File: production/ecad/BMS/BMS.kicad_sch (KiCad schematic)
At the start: 0 parts

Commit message: schematic draft merged w neha
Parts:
- added C1: 10u, Capacitor_SMD:C_0805_2012Metric, symbol Device:C
- added C2: 22u, Capacitor_SMD:C_0805_2012Metric, symbol Device:C
- added F1: 5A, Fuse:Fuse_0805_2012Metric, symbol Device:Fuse
- added J7, J9: Conn_01x02_Pin, Connector_PinHeader_2.54mm:PinHeader_1x02_P2.54mm_Vertical, symbol Connector:Conn_01x02_Pin
- added J8: XT60PW-M, CSTAR-MainBoard-Footprints:AMASS_XT60PW-M, symbol XT60PW-M:XT60PW-M
- added LED1, LED2: 150080VS75000, CSTAR-MainBoard-Footprints:LED_0VS75000_WRE, symbol 2024-02-25_19-51-49:150080VS75000
- added R1: 600, Resistor_SMD:R_0805_2012Metric, symbol Device:R_Small
- added R2: 260, Resistor_SMD:R_0805_2012Metric, symbol Device:R_Small
- added TP1: P5V, TestPoint:TestPoint_Pad_D2.0mm, symbol Connector:TestPoint
- added TP2: P3V3, TestPoint:TestPoint_Pad_D2.0mm, symbol Connector:TestPoint
- added U2: AZ1117IH-3.3TRG1, CSTAR-MainBoard-Footprints:SOT230P700X185-4N, symbol 2024-02-15_17-38-45:AZ1117IH-3.3TRG1
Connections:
- new net: C1.1, J9.1 (Pin_1), TP1.1, U2.3 (INPUT)
- new net: LED2.2, R2.2
- new net: LED1.2, R1.2
- new net: J7.2 (Pin_2), U2.4 (Vout)
- new net: F1.2, J9.2 (Pin_2)
- new net 3V3EXT: C2.1, J7.1 (Pin_1), R2.1, TP2.1, U2.2 (OUTPUT)
- new net 5VEXT: F1.1, R1.1
- new net BATT_IN: J8.1 (+)
- new net GND: C1.2, C2.2, LED1.1, LED2.1, U2.1 (GND)
- new net GNDEXT: J8.2 (-)
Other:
- removed sheet Power Sheet
- note added: "Add large resistors for LEDs for proper power dissipation in layout"
- note added: "Battery Connector"
- note added: "Green LED"
- note added: "LDO: 5V to 3.3V, 1A"
- note added: "Protection Circutry: Two 5A Protection Fuses to the 5V and 3v3 power rails. TVS Diode"

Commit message: feedback from Billayyy
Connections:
- net GNDEXT is gone; now on net GND: J8.2 (-)
- net 5VEXT renamed +5V
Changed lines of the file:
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@@
+	(wire
+		(pts
+			(xy 186.69 53.34) (xy 186.69 59.69)
+		)
+		(stroke
+			(width 0)
+			(type default)
+		)
+	)
 	(wire
 		(pts
@@
 		)
 	)
-	(hierarchical_label "GNDEXT"
+	(hierarchical_label "5VEXT"
+		(shape output)
+		(at 186.69 59.69 270)
+		(fields_autoplaced yes)
+		(effects
+			(font
+				(size 1.27 1.27)
+			)
+			(justify right)
+		)
+	)
+	(hierarchical_label "GND"
 		(shape input)
 		(at 41.91 125.73 270)
@@
 		)
 	)
+	(symbol
+		(lib_id "power:+5V")
+		(at 186.69 53.34 0)
+		(unit 1)
+		(exclude_from_sim no)
+		(in_bom yes)
+		(on_board yes)
+		(dnp no)
+		(fields_autoplaced yes)
+		(property "Reference" "#PWR08"
+			(at 186.69 57.15 0)
+			(effects
+				(font
+					(size 1.27 1.27)
+				)
+				(hide yes)
+			)
+		)
+		(property "Value" "+5V"
+			(at 186.69 48.26 0)
+			(effects
+				(font
+					(size 1.27 1.27)
+				)
+			)
+		)
+		(property "Footprint" ""
+			(at 186.69 53.34 0)
+			(effects
+				(font
+					(size 1.27 1.27)
+				)
+				(hide yes)
+			)
+		)
+		(property "Datasheet" ""
+			(at 186.69 53.34 0)
+			(effects
+				(font
+					(size 1.27 1.27)
+				)
+				(hide yes)
+			)
+		)
+		(property "Description" "Power symbol creates a global label with name \"+5V\""
+			(at 186.69 53.34 0)
+			(effects
+				(font
+					(size 1.27 1.27)
+				)
+				(hide yes)
+			)
+		)
+		(pin "1"
+		)
+		(instances
+			(project ""
+				(path "/a34d77bc-8f6a-417e-a206-3165e6c5c658/8907b1b2-1248-4544-8d7d-33764869f691"
+					(reference "#PWR08")
+					(unit 1)
+				)
+			)
+		)
+	)

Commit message: neha bms additions
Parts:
- removed F1: 5A, Fuse:Fuse_0805_2012Metric, symbol Device:Fuse
- removed J7, J9: Conn_01x02_Pin, Connector_PinHeader_2.54mm:PinHeader_1x02_P2.54mm_Vertical, symbol Connector:Conn_01x02_Pin
- removed J8: XT60PW-M, CSTAR-MainBoard-Footprints:AMASS_XT60PW-M, symbol XT60PW-M:XT60PW-M
- removed LED1, LED2: 150080VS75000, CSTAR-MainBoard-Footprints:LED_0VS75000_WRE, symbol 2024-02-25_19-51-49:150080VS75000
- removed R1: 600, Resistor_SMD:R_0805_2012Metric, symbol Device:R_Small
- removed R2: 260, Resistor_SMD:R_0805_2012Metric, symbol Device:R_Small
- removed TP1: P5V, TestPoint:TestPoint_Pad_D2.0mm, symbol Connector:TestPoint
- removed TP2: P3V3, TestPoint:TestPoint_Pad_D2.0mm, symbol Connector:TestPoint
- removed U2: AZ1117IH-3.3TRG1, CSTAR-MainBoard-Footprints:SOT230P700X185-4N, symbol 2024-02-15_17-38-45:AZ1117IH-3.3TRG1
- added R1: 30.1k, symbol Device:R
- added R2: 53.6k, symbol Device:R
- added R3: 250k, symbol Device:R
- added U3: TPS75233QPWPREP, TPS75233QPWPREP:TPS75233QPWPREP, symbol TPS75233QPWPREP:TPS75233QPWPREP
- C1: value 10u -> 47 uF; footprint Capacitor_SMD:C_0805_2012Metric -> (none)
- C2: value 22u -> 0.22 uF; footprint Capacitor_SMD:C_0805_2012Metric -> (none)
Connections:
- net 3V3EXT is gone; now on net +5V: C2.1
- net +5V: now also U3.P$3 (IN1), U3.P$4 (IN2)
- net GND: now also R2.2, U3.P$1 (GND/HEATSINK1), U3.P$10 (GND/HEATSINK2), U3.P$11 (GND/HEATSINK3), U3.P$17 (GND), U3.P$20 (GND/HEATSINK4), U3.P$5 (EN')
- net +3V3: now reaches C1.1
- net +3V3: now also R1.1, R2.1, R3.2, U3.P$7 (FB/SENSE), U3.P$9 (OUTPUT2)
- new net: R3.1, U3.P$6 (RESET'_OR_PG)
- new net: R1.2, U3.P$8 (OUTPUT1)
- no-connect marks 0 -> 8
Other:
- note added: "LDO: 5V to 3.3V, 2A"
- note removed: "Battery Connector"
- note removed: "Green LED"
- note removed: "LDO: 5V to 3.3V, 1A"

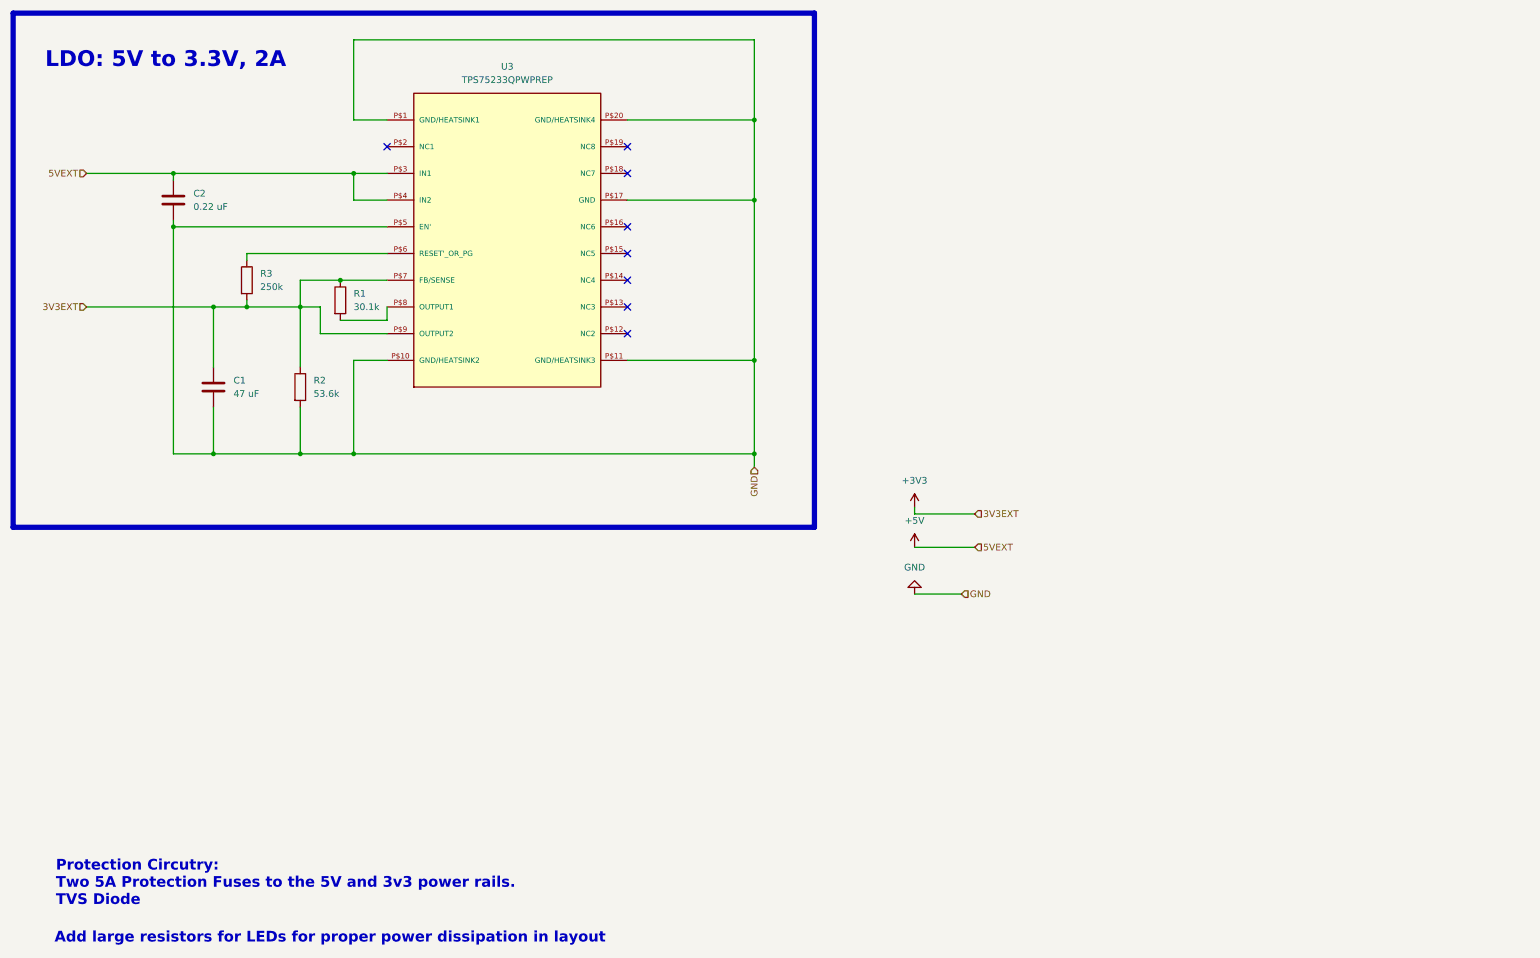
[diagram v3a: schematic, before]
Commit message: LDO schematic updated
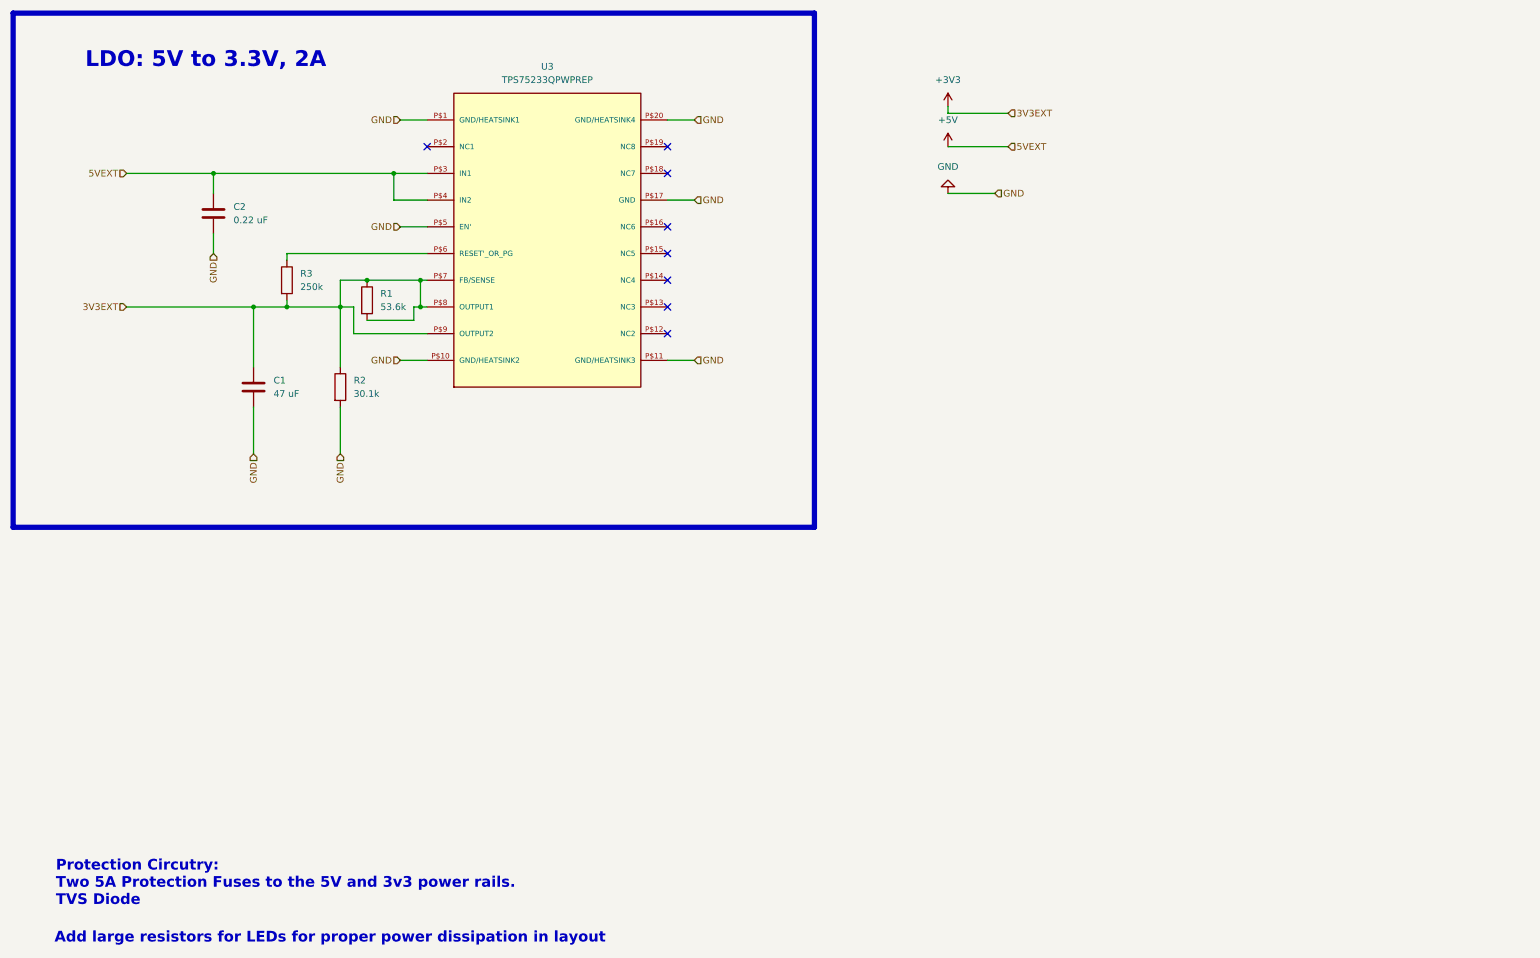
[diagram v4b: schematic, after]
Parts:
- R1: value 30.1k -> 53.6k
- R2: value 53.6k -> 30.1k
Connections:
- net +3V3: now also R1.2, U3.P$8 (OUTPUT1)
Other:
- moved on the sheet: C1, C2, R1, R2, R3, U3

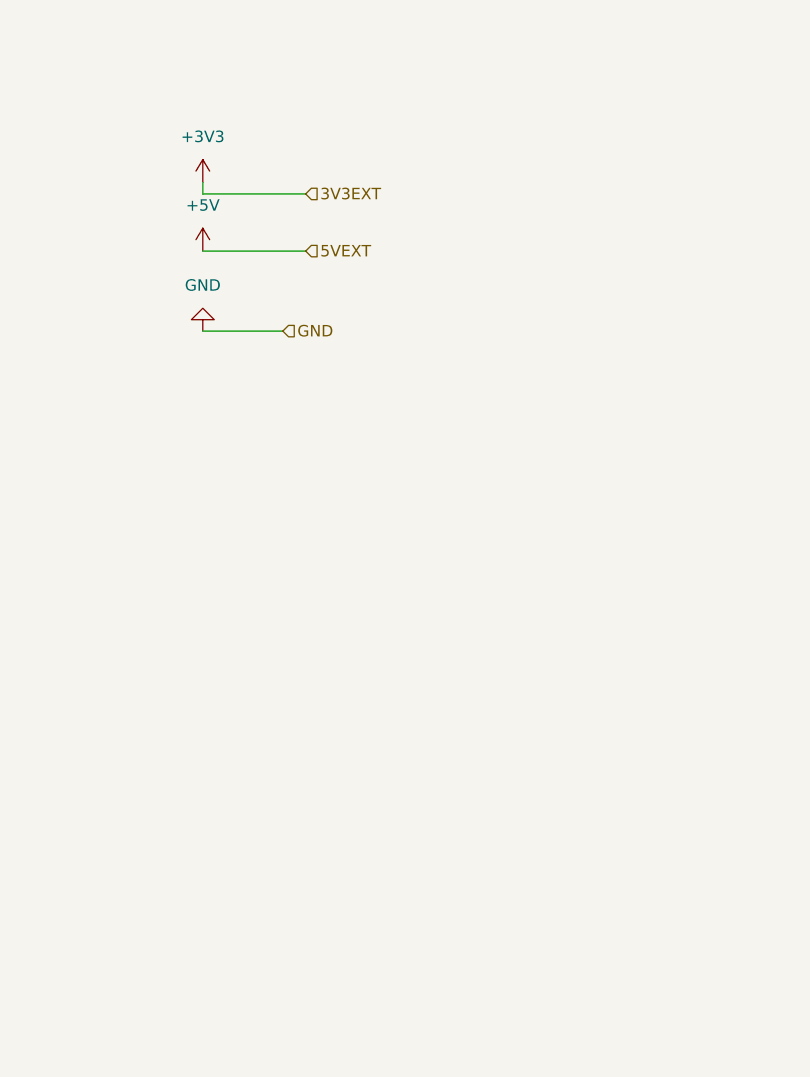
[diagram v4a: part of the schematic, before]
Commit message: Barrel jack added
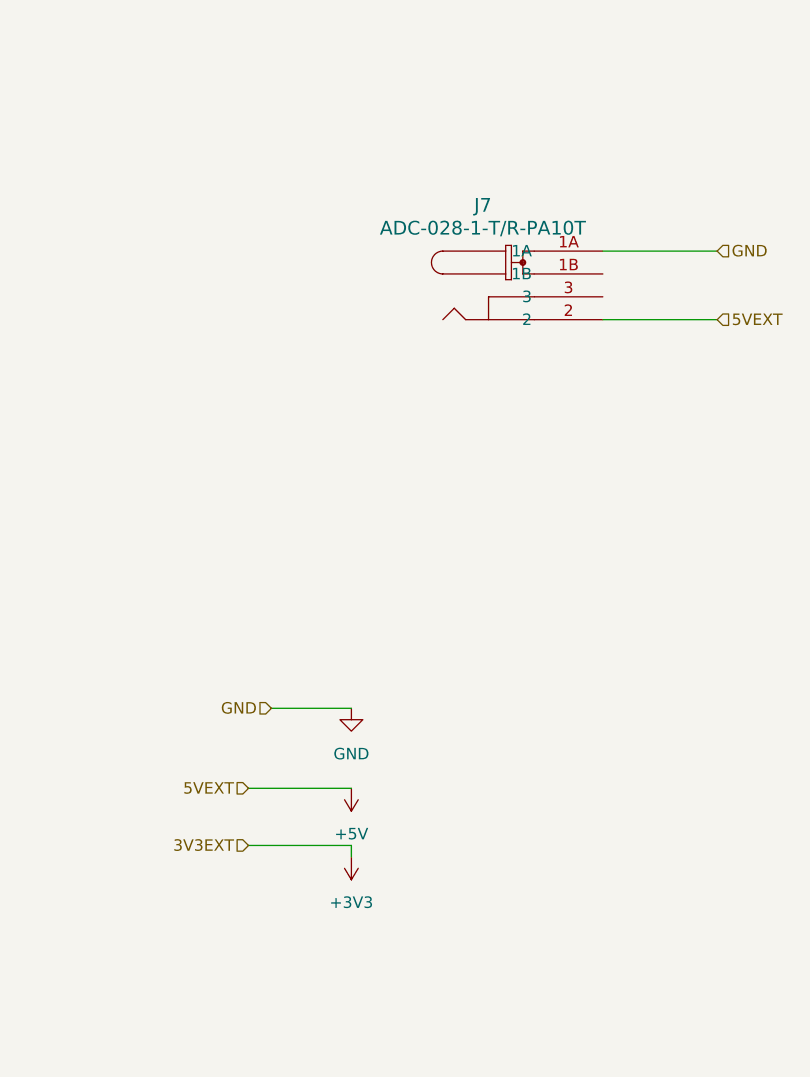
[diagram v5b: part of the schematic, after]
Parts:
- added J7: ADC-028-1-T/R-PA10T, ADC-028-x-T/R-PA10T_ADM, symbol 2024-10-20_20-22-38:ADC-028-1-T_R-PA10T
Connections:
- net +5V: now also J7.2
- net GND: now also J7.1A
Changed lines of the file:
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@@
 	(wire
 		(pts
-			(xy 194.31 41.91) (xy 205.74 41.91)
+			(xy 210.82 101.6) (xy 199.39 101.6)
 		)
 		(stroke
@@
 	(wire
 		(pts
+			(xy 238.76 49.53) (xy 251.46 49.53)
+		)
+		(stroke
+			(width 0)
+			(type default)
+		)
+	)
+	(wire
+		(pts
 			(xy 90.17 57.15) (xy 95.25 57.15)
 		)
@@
 	(wire
 		(pts
-			(xy 194.31 50.8) (xy 203.2 50.8)
+			(xy 210.82 92.71) (xy 201.93 92.71)
 		)
 		(stroke
@@
 	(wire
 		(pts
+			(xy 238.76 41.91) (xy 251.46 41.91)
+		)
+		(stroke
+			(width 0)
+			(type default)
+		)
+	)
+	(wire
+		(pts
 			(xy 140.97 82.55) (xy 146.05 82.55)
 		)
@@
 	(wire
 		(pts
-			(xy 194.31 35.56) (xy 205.74 35.56)
-		)
-		(stroke
-			(width 0)
-			(type default)
-		)
-	)
-	(wire
-		(pts
-			(xy 194.31 34.29) (xy 194.31 35.56)
+			(xy 210.82 107.95) (xy 199.39 107.95)
+		)
+		(stroke
+			(width 0)
+			(type default)
+		)
+	)
+	(wire
+		(pts
+			(xy 210.82 109.22) (xy 210.82 107.95)
 		)
 		(stroke
@@
 	(hierarchical_label "5VEXT"
 		(shape input)
-		(at 205.74 41.91 0)
+		(at 199.39 101.6 180)
+		(fields_autoplaced yes)
+		(effects
+			(font
+				(size 1.27 1.27)
+			)
+			(justify right)
+		)
+	)
+	(hierarchical_label "GND"
+		(shape input)
+		(at 78.74 100.33 270)
+		(fields_autoplaced yes)
+		(effects
+			(font
+				(size 1.27 1.27)
+			)
+			(justify right)
+		)
+	)
+	(hierarchical_label "GND"
+		(shape input)
+		(at 146.05 52.07 0)
 		(fields_autoplaced yes)
 		(effects
@@
 		)
 	)
+	(hierarchical_label "5VEXT"
+		(shape input)
+		(at 251.46 49.53 0)
+		(fields_autoplaced yes)
+		(effects
+			(font
+				(size 1.27 1.27)
+			)
+			(justify left)
+		)
+	)
 	(hierarchical_label "GND"
 		(shape input)
-		(at 78.74 100.33 270)
+		(at 146.05 82.55 0)
+		(fields_autoplaced yes)
+		(effects
+			(font
+				(size 1.27 1.27)
+			)
+			(justify left)
+		)
+	)
+	(hierarchical_label "GND"
+		(shape input)
+		(at 90.17 57.15 180)
 		(fields_autoplaced yes)
 		(effects
@@
 	(hierarchical_label "GND"
 		(shape input)
-		(at 146.05 52.07 0)
+		(at 251.46 41.91 0)
 		(fields_autoplaced yes)
 		(effects
@@
 		)
 	)
+	(hierarchical_label "3V3EXT"
+		(shape input)
+		(at 199.39 107.95 180)
+		(fields_autoplaced yes)
+		(effects
+			(font
+				(size 1.27 1.27)
+			)
+			(justify right)
+		)
+	)
 	(hierarchical_label "GND"
 		(shape input)
-		(at 146.05 82.55 0)
-		(fields_autoplaced yes)
-		(effects
-			(font
-				(size 1.27 1.27)
-			)
-			(justify left)
+		(at 201.93 92.71 180)
+		(fields_autoplaced yes)
+		(effects
+			(font
+				(size 1.27 1.27)
+			)
+			(justify right)
 		)
 	)
 	(hierarchical_label "GND"
 		(shape input)
-		(at 90.17 57.15 180)
+		(at 90.17 82.55 180)
 		(fields_autoplaced yes)
 		(effects
@@
 		)
 	)
-	(hierarchical_label "3V3EXT"
-		(shape input)
-		(at 205.74 35.56 0)
-		(fields_autoplaced yes)
-		(effects
-			(font
-				(size 1.27 1.27)
-			)
-			(justify left)
-		)
-	)
-	(hierarchical_label "GND"
-		(shape input)
-		(at 203.2 50.8 0)
-		(fields_autoplaced yes)
-		(effects
-			(font
-				(size 1.27 1.27)
-			)
-			(justify left)
-		)
-	)
-	(hierarchical_label "GND"
-		(shape input)
-		(at 90.17 82.55 180)
-		(fields_autoplaced yes)
-		(effects
-			(font
-				(size 1.27 1.27)
-			)
-			(justify right)
+	(symbol
+		(lib_id "2024-10-20_20-22-38:ADC-028-1-T_R-PA10T")
+		(at 238.76 41.91 0)
+		(unit 1)
+		(exclude_from_sim no)
+		(in_bom yes)
+		(on_board yes)
+		(dnp no)
+		(fields_autoplaced yes)
+		(property "Reference" "J7"
+			(at 225.4278 36.83 0)
+			(effects
+				(font
+					(size 1.524 1.524)
+				)
+			)
+		)
+		(property "Value" "ADC-028-1-T/R-PA10T"
+			(at 225.4278 39.37 0)
+			(effects
+				(font
+					(size 1.524 1.524)
+				)
+			)
+		)
+		(property "Footprint" "ADC-028-x-T/R-PA10T_ADM"
+			(at 238.76 41.91 0)
+			(effects
+				(font
+					(size 1.27 1.27)
+					(italic yes)
+				)
+				(hide yes)
+			)
+		)
+		(property "Datasheet" "ADC-028-1-T/R-PA10T"
+			(at 238.76 41.91 0)
+			(effects
+				(font
+					(size 1.27 1.27)
+					(italic yes)
+				)
+				(hide yes)
+			)
+		)
+		(property "Description" ""
+			(at 238.76 41.91 0)
+			(effects
+				(font
+					(size 1.27 1.27)
+				)
+				(hide yes)
+			)
+		)
+		(pin "1A"
+		)
+		(pin "1B"
+		)
+		(pin "3"
+		)
+		(pin "2"
+		)
+		(instances
+			(project "Main"
+				(path "/a34d77bc-8f6a-417e-a206-3165e6c5c658/8907b1b2-1248-4544-8d7d-33764869f691"
+					(reference "J7")
+					(unit 1)
+				)
+			)
 		)
 	)
@@
 	(symbol
 		(lib_id "power:+5V")
-		(at 194.31 41.91 0)
+		(at 210.82 101.6 180)
 		(unit 1)
 		(exclude_from_sim no)
@@
 		(fields_autoplaced yes)
 		(property "Reference" "#PWR03"
-			(at 194.31 45.72 0)
+			(at 210.82 97.79 0)
 			(effects
 				(font
@@
 		)
 		(property "Value" "+5V"
-			(at 194.31 36.83 0)
+			(at 210.82 106.68 0)
 			(effects
 				(font
@@
 		)
 		(property "Footprint" ""
-			(at 194.31 41.91 0)
+			(at 210.82 101.6 0)
 			(effects
 				(font
@@
 		)
 		(property "Datasheet" ""
-			(at 194.31 41.91 0)
+			(at 210.82 101.6 0)
 			(effects
 				(font
@@
 		)
 		(property "Description" "Power symbol creates a global label with name \"+5V\""
-			(at 194.31 41.91 0)
+			(at 210.82 101.6 0)
 			(effects
 				(font
@@
 	(symbol
 		(lib_id "power:GND")
-		(at 194.31 50.8 180)
+		(at 210.82 92.71 0)
 		(unit 1)
 		(exclude_from_sim no)
@@
 		(fields_autoplaced yes)
 		(property "Reference" "#PWR06"
-			(at 194.31 44.45 0)
+			(at 210.82 99.06 0)
 			(effects
 				(font
@@
 		)
 		(property "Value" "GND"
-			(at 194.31 45.72 0)
+			(at 210.82 97.79 0)
 			(effects
 				(font
@@
 		)
 		(property "Footprint" ""
-			(at 194.31 50.8 0)
+			(at 210.82 92.71 0)
 			(effects
 				(font
@@
 		)
 		(property "Datasheet" ""
-			(at 194.31 50.8 0)
+			(at 210.82 92.71 0)
 			(effects
 				(font
@@
 		)
 		(property "Description" "Power symbol creates a global label with name \"GND\" , ground"
-			(at 194.31 50.8 0)
+			(at 210.82 92.71 0)
 			(effects
 				(font
@@
 	(symbol
 		(lib_id "power:+3V3")
-		(at 194.31 34.29 0)
+		(at 210.82 109.22 180)
 		(unit 1)
 		(exclude_from_sim no)
@@
 		(fields_autoplaced yes)
 		(property "Reference" "#PWR02"
-			(at 194.31 38.1 0)
+			(at 210.82 105.41 0)
 			(effects
 				(font
@@
 		)
 		(property "Value" "+3V3"
-			(at 194.31 29.21 0)
+			(at 210.82 114.3 0)
 			(effects
 				(font
@@
 		)
 		(property "Footprint" ""
-			(at 194.31 34.29 0)
+			(at 210.82 109.22 0)
 			(effects
 				(font
@@
 		)
 		(property "Datasheet" ""
-			(at 194.31 34.29 0)
+			(at 210.82 109.22 0)
 			(effects
 				(font
@@
 		)
 		(property "Description" "Power symbol creates a global label with name \"+3V3\""
-			(at 194.31 34.29 0)
-			(effects
-				(font
+			(at 210.82 109.22 0)
+			(effects
+				(font
